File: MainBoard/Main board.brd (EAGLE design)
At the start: 100 x 100 mm, 10 parts

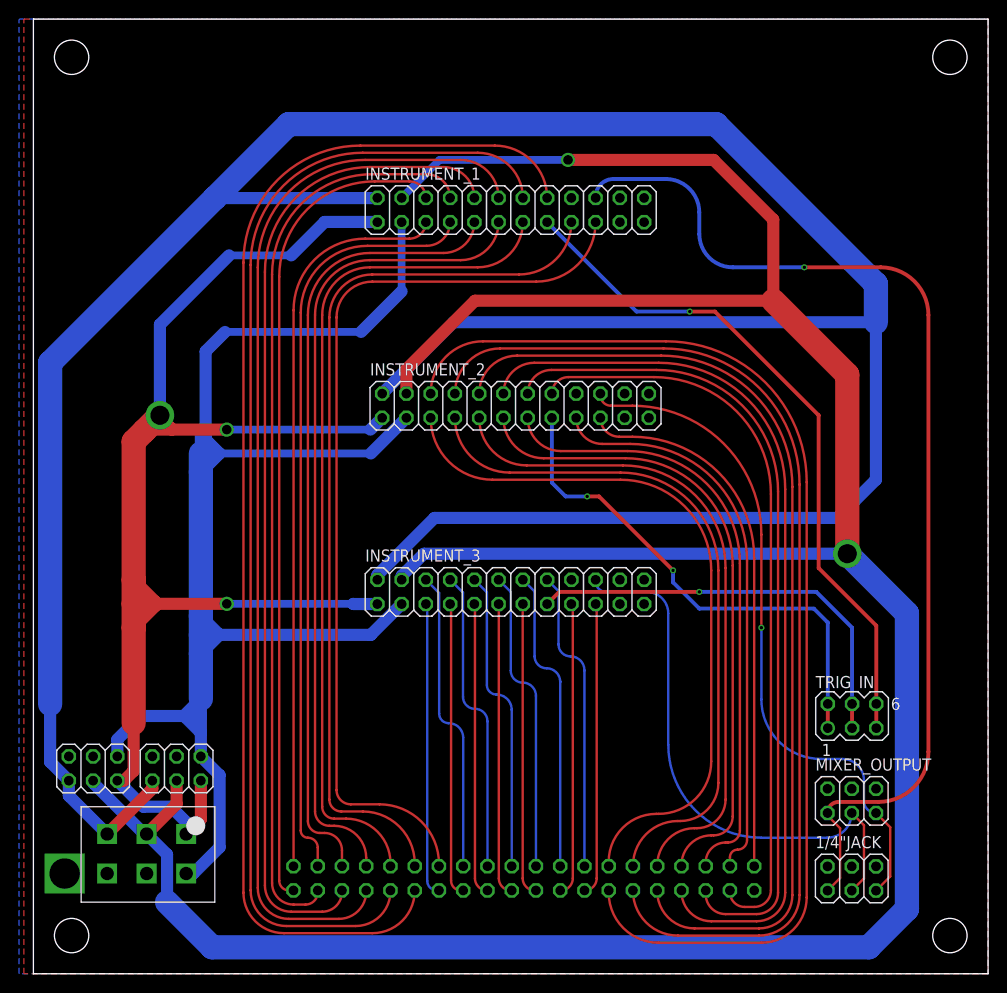
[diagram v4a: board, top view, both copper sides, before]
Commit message: Added silk screen
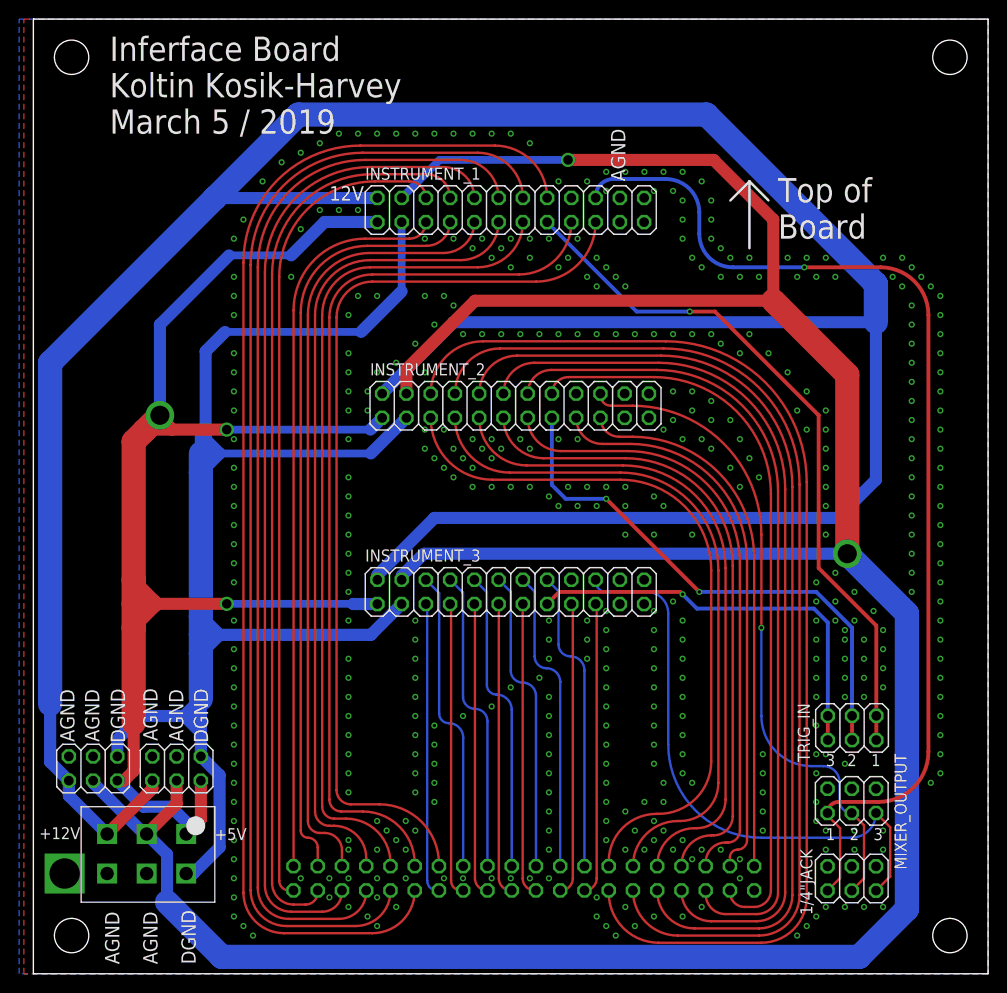
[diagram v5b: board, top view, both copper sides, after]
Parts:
- TRIG_IN: device con-lstb:MA03-2 -> pinhead:2X03
- moved TRIG_IN 1.25 mm to (85.8, 25.8)
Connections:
- net OUT2: now also INSTRUMENT_2.20; no longer INSTRUMENT_3.20
- net OUT3: now also INSTRUMENT_3.20; no longer INSTRUMENT_2.20
- net TRIG2: now also INSTRUMENT_2.15; no longer INSTRUMENT_3.15
- net TRIG3: now also INSTRUMENT_3.15; no longer INSTRUMENT_2.15
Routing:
- net TRIG2: track 44.5 -> 56.4 mm, vias 1 -> 2
- net TRIG3: track 53.6 -> 43.6 mm, vias 2 -> 1
- net OUT2: track 56.4 -> 65.9 mm, vias 0 -> 1
- net OUT3: track 68.4 -> 59.0 mm, vias 1 -> 0
- net TRIG1: track 72.1 -> 73.3 mm
- net -12V: track 317.3 -> 318.1 mm
- net +12V: track 312.4 -> 313.2 mm
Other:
- board text added: "+12V"
- board text added: "+5V"
- board text added: "1"
- board text added: "12V"
- board text added: "2"
- board text added: "3"
- board text added: "AGND"
- board text added: "DGND"
- board text added: "Inferface Board Koltin Kosik-Harvey March 5 / 2019"
- board text added: "Top of Board"
